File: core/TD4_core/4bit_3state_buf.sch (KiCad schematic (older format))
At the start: 2 parts, among them U34 74HC125

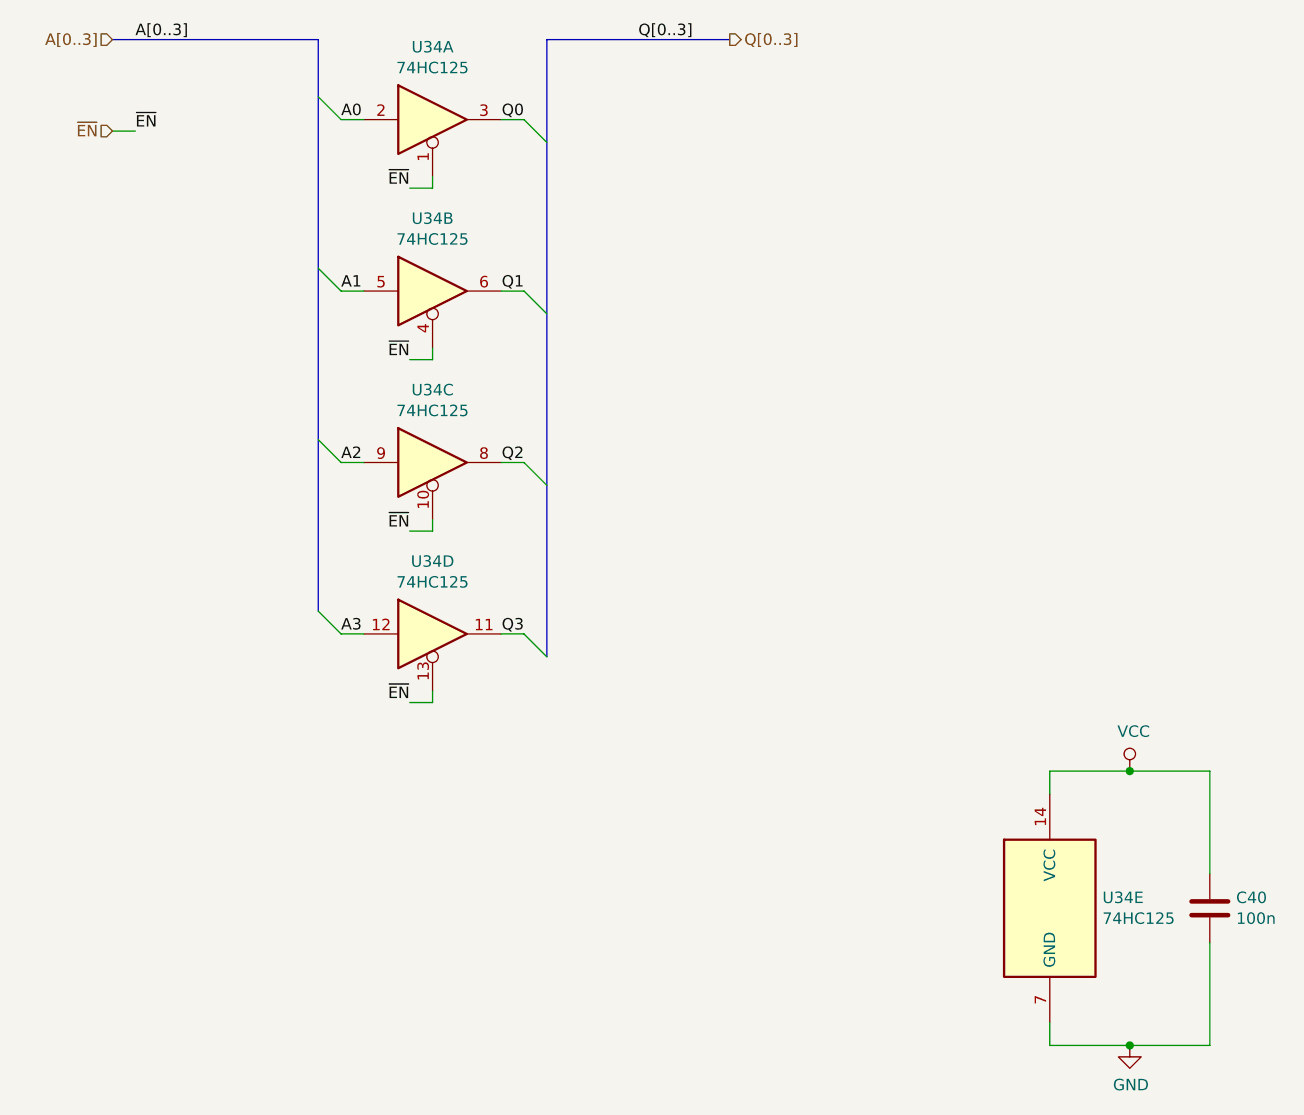
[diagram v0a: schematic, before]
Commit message: Replaced debug headers with vertical ones
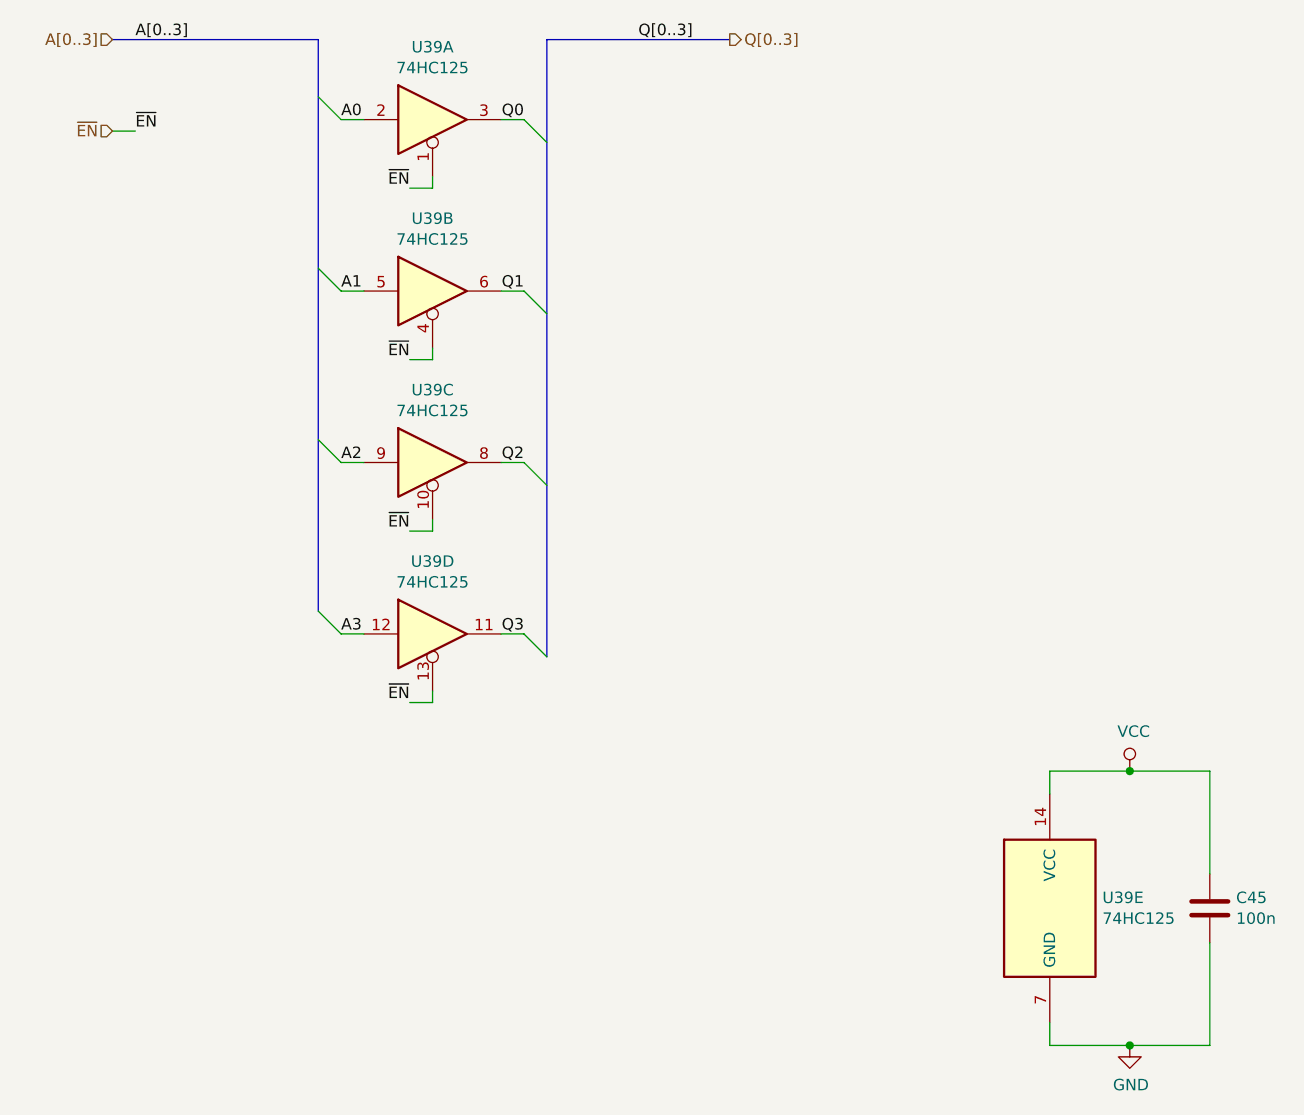
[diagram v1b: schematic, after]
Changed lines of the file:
@@
 AR Path="/5C758048/5C7339DC/5C662A4F" Ref="U?"  Part="1"
 AR Path="/5C77FFF0/5C780016/5C7339DC/5C662A4F" Ref="U40"  Part="1"
-F 0 "U34" H 5600 2567 50  0000 C CNN
+F 0 "U39" H 5600 2567 50  0000 C CNN
 F 1 "74HC125" H 5600 2476 50  0000 C CNN
 F 2 "Package_SO:SOIC-14_3.9x8.7mm_P1.27mm" H 5600 2250 50  0001 C CNN
@@
 AR Path="/5C758048/5C7339DC/5C662AA5" Ref="U?"  Part="2"
 AR Path="/5C77FFF0/5C780016/5C7339DC/5C662AA5" Ref="U40"  Part="2"
-F 0 "U34" H 5600 3317 50  0000 C CNN
+F 0 "U39" H 5600 3317 50  0000 C CNN
 F 1 "74HC125" H 5600 3226 50  0000 C CNN
 F 2 "Package_SO:SOIC-14_3.9x8.7mm_P1.27mm" H 5600 3000 50  0001 C CNN
@@
 AR Path="/5C758048/5C7339DC/5C662AD3" Ref="U?"  Part="3"
 AR Path="/5C77FFF0/5C780016/5C7339DC/5C662AD3" Ref="U40"  Part="3"
-F 0 "U34" H 5600 4067 50  0000 C CNN
+F 0 "U39" H 5600 4067 50  0000 C CNN
 F 1 "74HC125" H 5600 3976 50  0000 C CNN
 F 2 "Package_SO:SOIC-14_3.9x8.7mm_P1.27mm" H 5600 3750 50  0001 C CNN
@@
 AR Path="/5C758048/5C7339DC/5C662B05" Ref="U?"  Part="4"
 AR Path="/5C77FFF0/5C780016/5C7339DC/5C662B05" Ref="U40"  Part="4"
-F 0 "U34" H 5600 4817 50  0000 C CNN
+F 0 "U39" H 5600 4817 50  0000 C CNN
 F 1 "74HC125" H 5600 4726 50  0000 C CNN
 F 2 "Package_SO:SOIC-14_3.9x8.7mm_P1.27mm" H 5600 4500 50  0001 C CNN
@@
 AR Path="/5C758048/5C7339DC/5C662B31" Ref="U?"  Part="5"
 AR Path="/5C77FFF0/5C780016/5C7339DC/5C662B31" Ref="U40"  Part="5"
-F 0 "U34" H 8530 5746 50  0000 L CNN
+F 0 "U39" H 8530 5746 50  0000 L CNN
 F 1 "74HC125" H 8530 5655 50  0000 L CNN
 F 2 "Package_SO:SOIC-14_3.9x8.7mm_P1.27mm" H 8300 5700 50  0001 C CNN
@@
 AR Path="/5C758048/5C7339DC/5C6652A0" Ref="C?"  Part="1"
 AR Path="/5C77FFF0/5C780016/5C7339DC/5C6652A0" Ref="C46"  Part="1"
-F 0 "C40" H 9115 5746 50  0000 L CNN
+F 0 "C45" H 9115 5746 50  0000 L CNN
 F 1 "100n" H 9115 5655 50  0000 L CNN
 F 2 "Capacitor_SMD:C_0805_2012Metric" H 9038 5550 50  0001 C CNN
@@
 AR Path="/5C758048/5C7339DC/5C6657D0" Ref="#PWR?"  Part="1"
 AR Path="/5C77FFF0/5C780016/5C7339DC/5C6657D0" Ref="#PWR0147"  Part="1"
-F 0 "#PWR0129" H 8650 4950 50  0001 C CNN
+F 0 "#PWR0147" H 8650 4950 50  0001 C CNN
 F 1 "VCC" H 8667 5273 50  0000 C CNN
 F 2 "" H 8650 5100 50  0001 C CNN
@@
 AR Path="/5C758048/5C7339DC/5C66581B" Ref="#PWR?"  Part="1"
 AR Path="/5C77FFF0/5C780016/5C7339DC/5C66581B" Ref="#PWR0148"  Part="1"
-F 0 "#PWR0130" H 8650 6050 50  0001 C CNN
+F 0 "#PWR0148" H 8650 6050 50  0001 C CNN
 F 1 "GND" H 8655 6127 50  0000 C CNN
 F 2 "" H 8650 6300 50  0001 C CNN
